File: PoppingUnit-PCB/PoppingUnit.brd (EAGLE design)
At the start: 95 x 63 mm, 78 parts, among them IC2 7805DT, J1 RS485, J2 POWER_JACKPTH, Q1 16MHz 10ppm, U1 ARDUINO_LEONARDO-REV3B_SMARTP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, U2 SN75176ASOIC, X1 USBPTH

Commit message: Update popping unit to RevB (should be good to go!)
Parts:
- removed J1: RS485, con-amp:520426-4
- added J3: (no value), con-amp:555153-1
- added LED2: (no value), SparkFun:LED5MM
- added R18: 1k, adafruit:R0603
- moved LED1 18.9 mm to (18.0, 37.8)
- moved C1 0.50 mm to (14.6, 45.2)
- moved C2 0.50 mm to (16.5, 42.8)
- moved C22 0.50 mm to (19.8, 41.0)
- moved C3 0.50 mm to (26.5, 53.5)
- moved C4 0.50 mm to (24.8, 54.5)
- moved C5 0.50 mm to (29.5, 43.5)
- moved C6 0.50 mm to (16.0, 48.6)
- moved C7 0.50 mm to (23.8, 8.50)
- moved C8 0.50 mm to (23.0, 53.5)
- moved R1 0.50 mm to (21.0, 12.2)
- moved R2 0.50 mm to (27.8, 8.50)
- moved R4 0.50 mm to (16.0, 54.5)
- moved R5 0.50 mm to (16.0, 52.8)
- moved R6 0.50 mm to (16.0, 51.0)
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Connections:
- net SIG0 renamed OUT_5
- net SIG1 renamed OUT_6
- net SIG10 renamed OUT_15
- net SIG11 renamed OUT_16
- net SIG12 renamed OUT_4
- net SIG13 renamed OUT_3
- net SIG14 renamed OUT_2
- net SIG2 renamed OUT_7
- net SIG3 renamed OUT_8
- net SIG4 renamed OUT_12
- net SIG5 renamed OUT_11
- net SIG6 renamed OUT_10
- net SIG7 renamed OUT_9
- net SIG8 renamed OUT_13
- net SIG9 renamed OUT_14
- removed net SIG15: R22.2, U$18.P$1, U1.33
- new net OUT_1: R22.2, U$18.P$1, U1.21
- new net STATUS_1: R18.2, U1.19
- net GND: now also J3.7, J3.8, LED2.K; no longer J1.7, J1.8
- net N$12: now also LED2.A, R18.1; no longer U1.21
- net RS485A: now also J3.1; no longer J1.1
- net RS485B: now also J3.2; no longer J1.2
- net VIN: now also J3.4, J3.5; no longer J1.4, J1.5
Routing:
- net OUT_1: track 0.00 -> 61.4 mm, vias 0 -> 4
- net SIG15: track 51.9 -> 0.00 mm, vias 2 -> 0
- net N$8: track 27.2 -> 4.80 mm
- net STATUS_1: track 0.00 -> 11.1 mm, vias 0 -> 2
- net N$12: track 0.00 -> 10.6 mm
- net RS485B: track 11.2 -> 13.2 mm
- net RS485A: track 12.9 -> 14.9 mm
- net RX: track 45.9 -> 46.6 mm
- net OUT_9: track 75.6 -> 75.1 mm
- net OUT_8: track 110.7 -> 110.2 mm
- net OUT_7: track 102.3 -> 101.8 mm
- net OUT_6: track 93.8 -> 93.3 mm
- net OUT_5: track 85.3 -> 84.8 mm
- net OUT_4: track 76.8 -> 76.3 mm
- net OUT_3: track 68.3 -> 67.8 mm
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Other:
- board text added: "RevB 3/8"
- board text removed: "RevA 3/2"

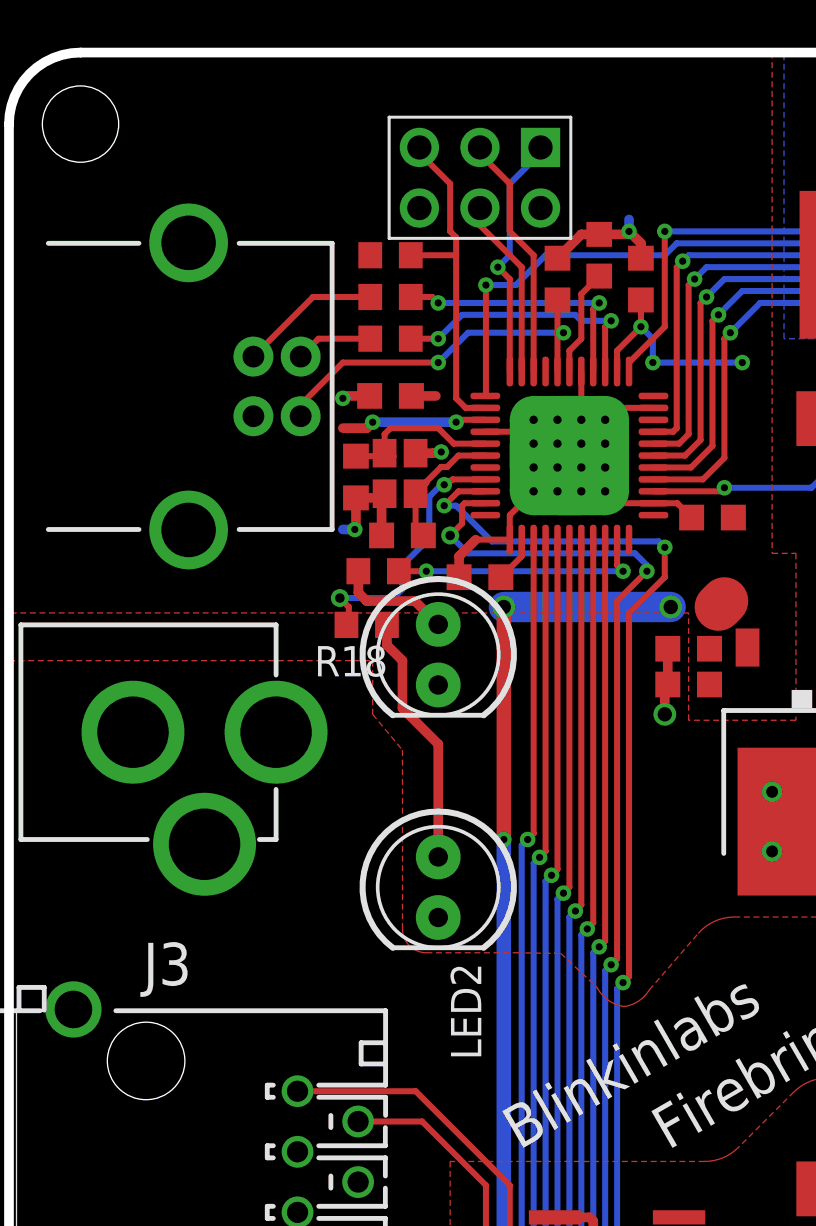
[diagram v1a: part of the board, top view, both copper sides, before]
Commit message: Update Popping Unit PCB for release, send to board house
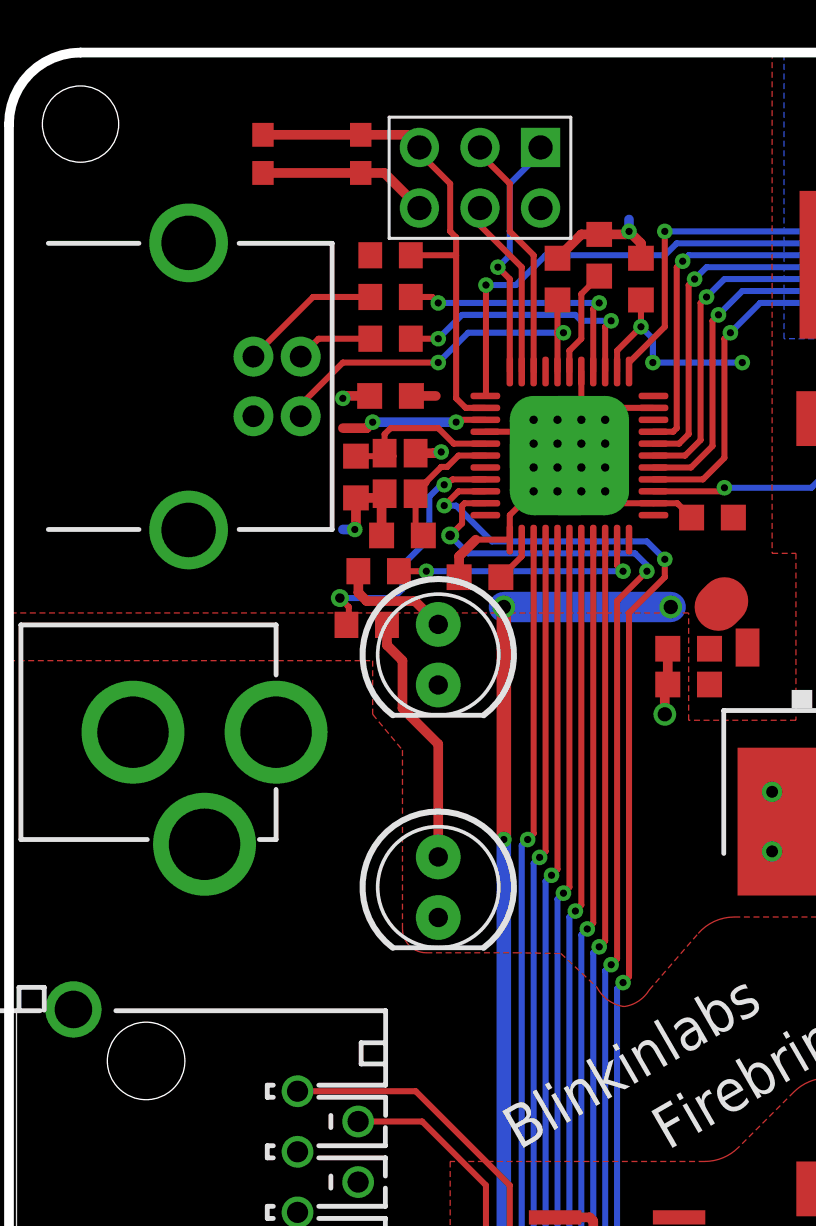
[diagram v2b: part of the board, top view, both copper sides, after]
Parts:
- added U$20: (no value), blinkinlabs:BUTTON_MOMENTARY_KMR211G
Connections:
- net GND: now also U$20.P$1, U$20.P$2
- net RESET: now also U$20.P$3, U$20.P$4
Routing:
- net GND: track 132.8 -> 140.0 mm
- net RESET: track 14.4 -> 21.2 mm
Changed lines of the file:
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@@
 <layer number="19" name="Unrouted" color="13" fill="1" visible="yes" active="yes"/>
 <layer number="20" name="Dimension" color="15" fill="1" visible="yes" active="yes"/>
-<layer number="21" name="tPlace" color="7" fill="1" visible="yes" active="yes"/>
-<layer number="22" name="bPlace" color="7" fill="1" visible="yes" active="yes"/>
-<layer number="23" name="tOrigins" color="15" fill="1" visible="yes" active="yes"/>
-<layer number="24" name="bOrigins" color="15" fill="1" visible="yes" active="yes"/>
+<layer number="21" name="tPlace" color="7" fill="1" visible="no" active="yes"/>
+<layer number="22" name="bPlace" color="7" fill="1" visible="no" active="yes"/>
+<layer number="23" name="tOrigins" color="15" fill="1" visible="no" active="yes"/>
+<layer number="24" name="bOrigins" color="15" fill="1" visible="no" active="yes"/>
 <layer number="25" name="tNames" color="7" fill="1" visible="yes" active="yes"/>
 <layer number="26" name="bNames" color="7" fill="1" visible="yes" active="yes"/>
-<layer number="27" name="tValues" color="7" fill="1" visible="no" active="yes"/>
-<layer number="28" name="bValues" color="7" fill="1" visible="no" active="yes"/>
+<layer number="27" name="tValues" color="7" fill="1" visible="yes" active="yes"/>
+<layer number="28" name="bValues" color="7" fill="1" visible="yes" active="yes"/>
 <layer number="29" name="tStop" color="7" fill="3" visible="no" active="yes"/>
 <layer number="30" name="bStop" color="7" fill="6" visible="no" active="yes"/>
 <layer number="31" name="tCream" color="7" fill="4" visible="no" active="yes"/>
-<layer number="32" name="bCream" color="7" fill="5" visible="yes" active="yes"/>
+<layer number="32" name="bCream" color="7" fill="5" visible="no" active="yes"/>
 <layer number="33" name="tFinish" color="6" fill="3" visible="no" active="yes"/>
 <layer number="34" name="bFinish" color="6" fill="6" visible="no" active="yes"/>
@@
 </element>
 <element name="U$19" library="blinkinlabs" package="DSN2596" value="DC_DC" x="65" y="31.5" smashed="yes"/>
-<element name="J3" library="con-amp" package="555153-1" value="" x="5.75" y="15" rot="R270"/>
-<element name="R18" library="adafruit" package="R0603" value="1k" x="15" y="39" rot="R180"/>
-<element name="LED2" library="SparkFun" package="LED5MM" value="" x="18" y="28" rot="R270"/>
+<element name="J3" library="con-amp" package="555153-1" value="" x="5.75" y="15" smashed="yes" rot="R270">
+<attribute name="VALUE" x="5.623" y="4.84" size="1.778" layer="27"/>
+</element>
+<element name="R18" library="adafruit" package="R0603" value="1k" x="15" y="39" smashed="yes" rot="R180"/>
+<element name="LED2" library="SparkFun" package="LED5MM" value="" x="18" y="28" smashed="yes" rot="R270">
+<attribute name="VALUE" x="16.1966" y="24.7996" size="1.27" layer="27" ratio="10" rot="R270"/>
+</element>
+<element name="U$20" library="blinkinlabs" package="BUTTON_MOMENTARY_KMR211G" value="" x="12.75" y="58.75" smashed="yes" rot="R180">
+<attribute name="VALUE" x="15.75" y="61.75" size="1.27" layer="27" rot="R180"/>
+</element>
 </elements>
 <signals>
@@
 <contactref element="J3" pad="8"/>
 <contactref element="LED2" pad="K"/>
+<contactref element="U$20" pad="P$2"/>
+<contactref element="U$20" pad="P$1"/>
+<wire x1="14.75" y1="57.95" x2="15.74" y2="57.95" width="0.4064" layer="1"/>
+<wire x1="15.74" y1="57.95" x2="17.21" y2="56.48" width="0.4064" layer="1"/>
+<wire x1="14.75" y1="57.95" x2="10.65" y2="57.95" width="0.4064" layer="1"/>
 </signal>
 <signal name="RX">
@@
 <wire x1="18.25" y1="44" x2="18.75" y2="44" width="0.254" layer="16"/>
 <wire x1="18.75" y1="44" x2="20.25" y2="42.5" width="0.254" layer="16"/>
-<wire x1="20.25" y1="42.5" x2="27.25" y2="42.5" width="0.254" layer="16"/>
-<wire x1="27.25" y1="42.5" x2="27.5" y2="42.25" width="0.254" layer="16"/>
-<via x="27.5" y="42.25" extent="1-16" drill="0.3"/>
-<wire x1="27.5" y1="42.25" x2="27.5" y2="41" width="0.254" layer="1"/>
+<wire x1="20.25" y1="42.5" x2="26.75" y2="42.5" width="0.254" layer="16"/>
+<wire x1="26.75" y1="42.5" x2="27.5" y2="41.75" width="0.254" layer="16"/>
+<via x="27.5" y="41.75" extent="1-16" drill="0.3"/>
+<wire x1="27.5" y1="41.75" x2="27.5" y2="41" width="0.254" layer="1"/>
 <wire x1="27.5" y1="41" x2="26" y2="39.5" width="0.254" layer="1"/>
 <wire x1="26" y1="39.5" x2="26" y2="24.25" width="0.254" layer="1"/>
@@
 <wire x1="19.975" y1="48.1" x2="19.15" y2="48.1" width="0.254" layer="1"/>
 <wire x1="16.85" y1="54.5" x2="18.75" y2="54.5" width="0.254" layer="1"/>
+<contactref element="U$20" pad="P$4"/>
+<contactref element="U$20" pad="P$3"/>
+<wire x1="14.75" y1="59.55" x2="16.68" y2="59.55" width="0.4064" layer="1"/>
+<wire x1="16.68" y1="59.55" x2="17.21" y2="59.02" width="0.4064" layer="1"/>
+<wire x1="10.65" y1="59.55" x2="14.75" y2="59.55" width="0.4064" layer="1"/>
 </signal>
 <signal name="N$8">
@@
 <wire x1="19.975" y1="47.6" x2="18.6" y2="47.6" width="0.254" layer="1"/>
 <wire x1="18.6" y1="47.6" x2="18.75" y2="47.5" width="0.254" layer="1"/>
-<wire x1="27.025" y1="43.6" x2="30.375" y2="43.5" width="0" layer="19" extent="1-1"/>
 </signal>
 <signal name="N$7">

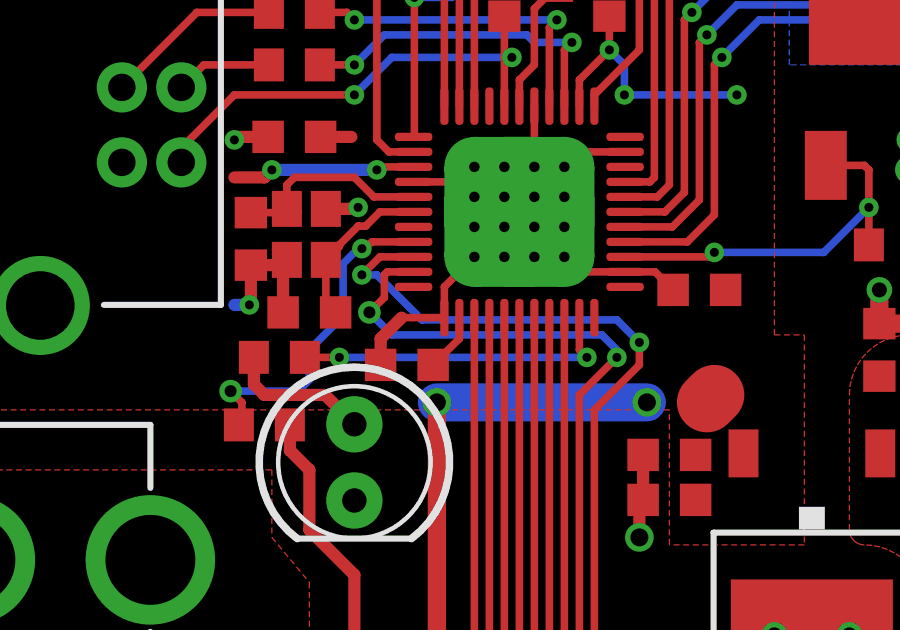
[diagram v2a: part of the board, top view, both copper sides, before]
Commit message: Update PoppingUnit board to fix bummer mistake (Arduino remuxes TX, so don't use it as an output channel), update firmware to match
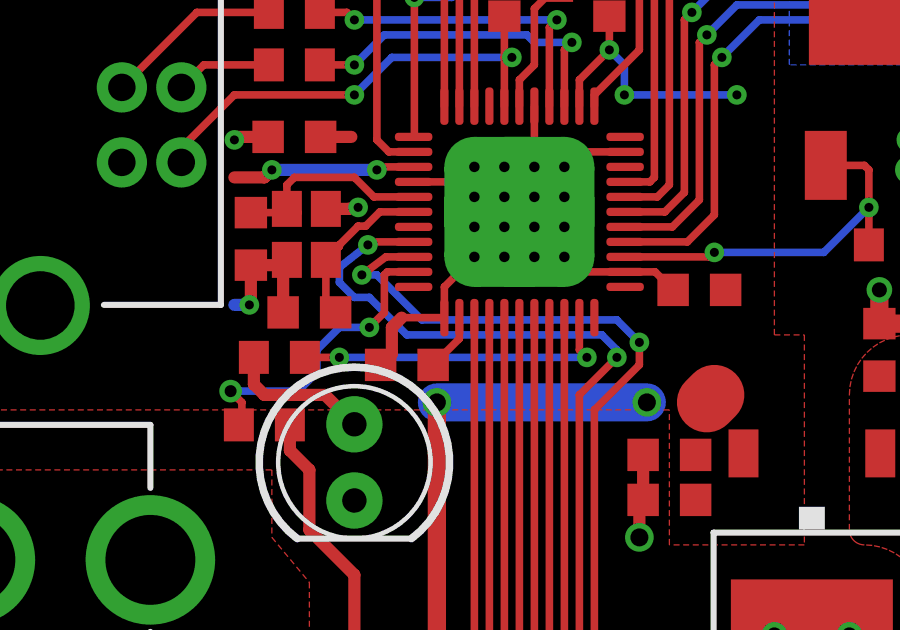
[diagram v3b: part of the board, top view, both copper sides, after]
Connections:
- net OUT_1: now also U1.19; no longer U1.21
- net STATUS_1: now also U1.21; no longer U1.19
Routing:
- net OUT_1: track 61.4 -> 63.9 mm
- net STATUS_1: track 11.1 -> 10.2 mm
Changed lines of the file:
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@@
 <layer number="19" name="Unrouted" color="13" fill="1" visible="yes" active="yes"/>
 <layer number="20" name="Dimension" color="15" fill="1" visible="yes" active="yes"/>
-<layer number="21" name="tPlace" color="7" fill="1" visible="no" active="yes"/>
-<layer number="22" name="bPlace" color="7" fill="1" visible="no" active="yes"/>
-<layer number="23" name="tOrigins" color="15" fill="1" visible="no" active="yes"/>
-<layer number="24" name="bOrigins" color="15" fill="1" visible="no" active="yes"/>
+<layer number="21" name="tPlace" color="7" fill="1" visible="yes" active="yes"/>
+<layer number="22" name="bPlace" color="7" fill="1" visible="yes" active="yes"/>
+<layer number="23" name="tOrigins" color="15" fill="1" visible="yes" active="yes"/>
+<layer number="24" name="bOrigins" color="15" fill="1" visible="yes" active="yes"/>
 <layer number="25" name="tNames" color="7" fill="1" visible="yes" active="yes"/>
 <layer number="26" name="bNames" color="7" fill="1" visible="yes" active="yes"/>
@@
 <wire x1="27.025" y1="44.1" x2="28.025" y2="44.1" width="0.254" layer="1"/>
 <wire x1="28.025" y1="44.1" x2="28.625" y2="43.5" width="0.254" layer="1"/>
-<wire x1="18.875" y1="41" x2="18.875" y2="41.875" width="0.4064" layer="1"/>
-<wire x1="18.875" y1="41.875" x2="19.575" y2="42.575" width="0.4064" layer="1"/>
-<wire x1="21" y1="42.575" x2="19.575" y2="42.575" width="0.254" layer="1"/>
 <via x="14" y="48.5" extent="1-16" drill="0.3"/>
 <wire x1="14.55" y1="44.325" x2="14.55" y2="43.05" width="0.4064" layer="1"/>
@@
 <wire x1="15.74" y1="57.95" x2="17.21" y2="56.48" width="0.4064" layer="1"/>
 <wire x1="14.75" y1="57.95" x2="10.65" y2="57.95" width="0.4064" layer="1"/>
+<wire x1="21" y1="42.575" x2="19.575" y2="42.575" width="0.254" layer="1"/>
+<wire x1="19.575" y1="42.575" x2="19.25" y2="42.25" width="0.4064" layer="1"/>
+<wire x1="19.25" y1="42.25" x2="19.25" y2="41.375" width="0.4064" layer="1"/>
+<wire x1="19.25" y1="41.375" x2="18.875" y2="41" width="0.4064" layer="1"/>
 </signal>
 <signal name="RX">
@@
 <wire x1="25.75" y1="12.25" x2="25.5" y2="12.5" width="0.254" layer="16"/>
 <wire x1="25.5" y1="12.5" x2="25.5" y2="23.75" width="0.254" layer="16"/>
-<wire x1="19.975" y1="44.6" x2="18.85" y2="44.6" width="0.254" layer="1"/>
-<wire x1="18.85" y1="44.6" x2="18.25" y2="44" width="0.254" layer="1"/>
+<wire x1="19.975" y1="44.6" x2="19.05" y2="44.6" width="0.254" layer="1"/>
+<wire x1="19.05" y1="44.6" x2="18.25" y2="44" width="0.254" layer="1"/>
 <via x="18.25" y="44" extent="1-16" drill="0.3"/>
-<wire x1="18.25" y1="44" x2="18.75" y2="44" width="0.254" layer="16"/>
-<wire x1="18.75" y1="44" x2="20.25" y2="42.5" width="0.254" layer="16"/>
 <wire x1="20.25" y1="42.5" x2="26.75" y2="42.5" width="0.254" layer="16"/>
 <wire x1="26.75" y1="42.5" x2="27.5" y2="41.75" width="0.254" layer="16"/>
@@
 <via x="25.75" y="24" extent="1-16" drill="0.3"/>
 <wire x1="25.5" y1="23.75" x2="25.75" y2="24" width="0.254" layer="16"/>
+<wire x1="20.25" y1="42.5" x2="18.75" y2="44" width="0.254" layer="16"/>
+<wire x1="18.75" y1="44" x2="18.25" y2="44" width="0.254" layer="16"/>
 </signal>
 <signal name="MOSI">
@@
 <via x="25.25" y="24.75" extent="1-16" drill="0.3"/>
 <wire x1="25" y1="24.5" x2="25.25" y2="24.75" width="0.254" layer="16"/>
-<contactref element="U1" pad="21"/>
-<wire x1="19.975" y1="44.1" x2="19.1" y2="44.1" width="0.254" layer="1"/>
-<wire x1="19.1" y1="44.1" x2="19" y2="44" width="0.254" layer="1"/>
-<wire x1="19" y1="44" x2="19" y2="43.25" width="0.254" layer="1"/>
-<wire x1="19" y1="43.25" x2="18.5" y2="42.75" width="0.254" layer="1"/>
-<via x="18.5" y="42.75" extent="1-16" drill="0.4"/>
-<wire x1="18.5" y1="42.75" x2="19.25" y2="42" width="0.254" layer="16"/>
-<wire x1="19.25" y1="42" x2="26.25" y2="42" width="0.254" layer="16"/>
+<wire x1="19.75" y1="42" x2="26.25" y2="42" width="0.254" layer="16"/>
 <wire x1="26.25" y1="42" x2="26.75" y2="41.5" width="0.254" layer="16"/>
 <wire x1="26.75" y1="41.5" x2="26.75" y2="41.25" width="0.254" layer="16"/>
 <via x="26.75" y="41.25" extent="1-16" drill="0.3"/>
+<contactref element="U1" pad="19"/>
+<wire x1="19.975" y1="45.1" x2="18.35" y2="45.1" width="0.254" layer="1"/>
+<wire x1="18.35" y1="45.1" x2="18.45" y2="45" width="0.254" layer="1"/>
+<via x="18.45" y="45" extent="1-16" drill="0.3"/>
+<wire x1="18.45" y1="45" x2="17.5" y2="44.25" width="0.254" layer="16"/>
+<wire x1="17.5" y1="44.25" x2="17.5" y2="43.75" width="0.254" layer="16"/>
+<wire x1="17.5" y1="43.75" x2="18" y2="43.25" width="0.254" layer="16"/>
+<wire x1="18" y1="43.25" x2="18.5" y2="43.25" width="0.254" layer="16"/>
+<wire x1="18.5" y1="43.25" x2="19.75" y2="42" width="0.254" layer="16"/>
 </signal>
 <signal name="5V">
@@
 </signal>
 <signal name="STATUS_1">
-<contactref element="U1" pad="19"/>
 <contactref element="R18" pad="2"/>
-<wire x1="19.975" y1="45.1" x2="18.6" y2="45.1" width="0.254" layer="1"/>
-<wire x1="18.6" y1="45.1" x2="18.25" y2="44.875" width="0.254" layer="1"/>
-<via x="18.25" y="44.875" extent="1-16" drill="0.3"/>
-<wire x1="18.25" y1="44.875" x2="18.125" y2="44.875" width="0.254" layer="16"/>
-<wire x1="18.125" y1="44.875" x2="17.625" y2="44.375" width="0.254" layer="16"/>
-<wire x1="17.625" y1="44.375" x2="17.625" y2="42.625" width="0.254" layer="16"/>
-<wire x1="17.625" y1="42.625" x2="16.5" y2="41.5" width="0.254" layer="16"/>
-<wire x1="16.5" y1="41.5" x2="16.5" y2="40.5" width="0.254" layer="16"/>
-<wire x1="16.5" y1="40.5" x2="16.125" y2="40.125" width="0.254" layer="16"/>
+<wire x1="16.75" y1="41.5" x2="16.75" y2="40.75" width="0.254" layer="16"/>
+<wire x1="16.75" y1="40.75" x2="16.125" y2="40.125" width="0.254" layer="16"/>
 <wire x1="16.125" y1="40.125" x2="13.875" y2="40.125" width="0.254" layer="16"/>
 <via x="13.875" y="40.125" extent="1-16" drill="0.4"/>
@@
 <wire x1="14.25" y1="39.75" x2="14.25" y2="39.1" width="0.254" layer="1"/>
 <wire x1="14.25" y1="39.1" x2="14.15" y2="39" width="0.254" layer="1"/>
+<contactref element="U1" pad="21"/>
+<wire x1="19.975" y1="44.1" x2="19.1" y2="44.1" width="0.254" layer="1"/>
+<wire x1="19.1" y1="44.1" x2="19" y2="44" width="0.254" layer="1"/>
+<wire x1="19" y1="44" x2="19" y2="42.75" width="0.254" layer="1"/>
+<wire x1="19" y1="42.75" x2="18.5" y2="42.25" width="0.254" layer="1"/>
+<via x="18.5" y="42.25" extent="1-16" drill="0.3"/>
+<wire x1="18.5" y1="42.25" x2="17.5" y2="42.25" width="0.254" layer="16"/>
+<wire x1="17.5" y1="42.25" x2="16.75" y2="41.5" width="0.254" layer="16"/>
 </signal>
 <signal name="N$12">
